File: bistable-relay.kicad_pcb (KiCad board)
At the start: 2 copper layers, 28.8 x 12.9 mm, 11 parts, among them J1 edge_connector, K1 Fujitsu_FTR-F1A, U1 MIC4427

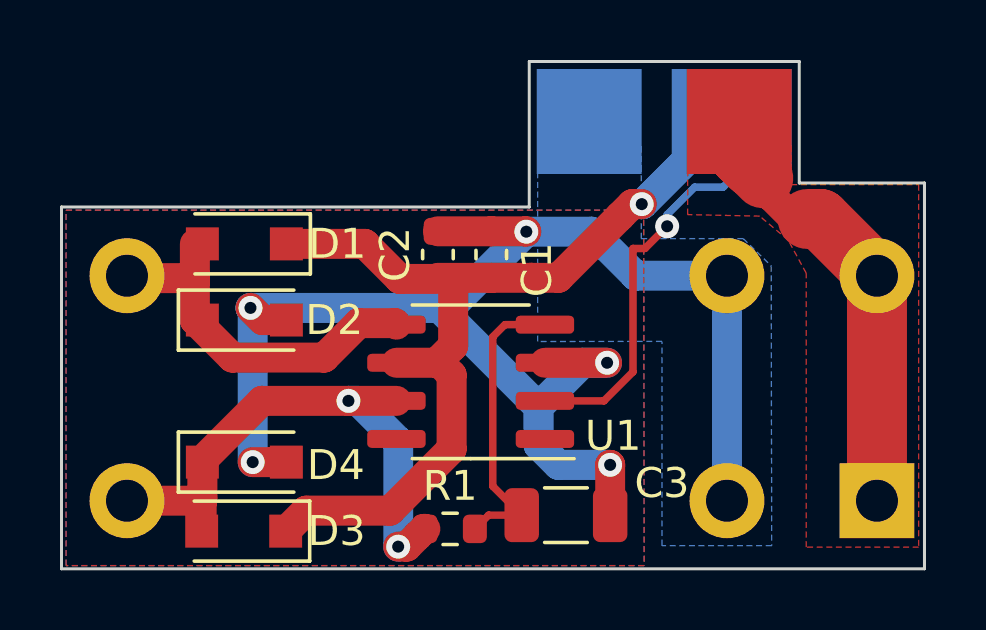
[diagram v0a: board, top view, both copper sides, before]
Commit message: use FH44L relay
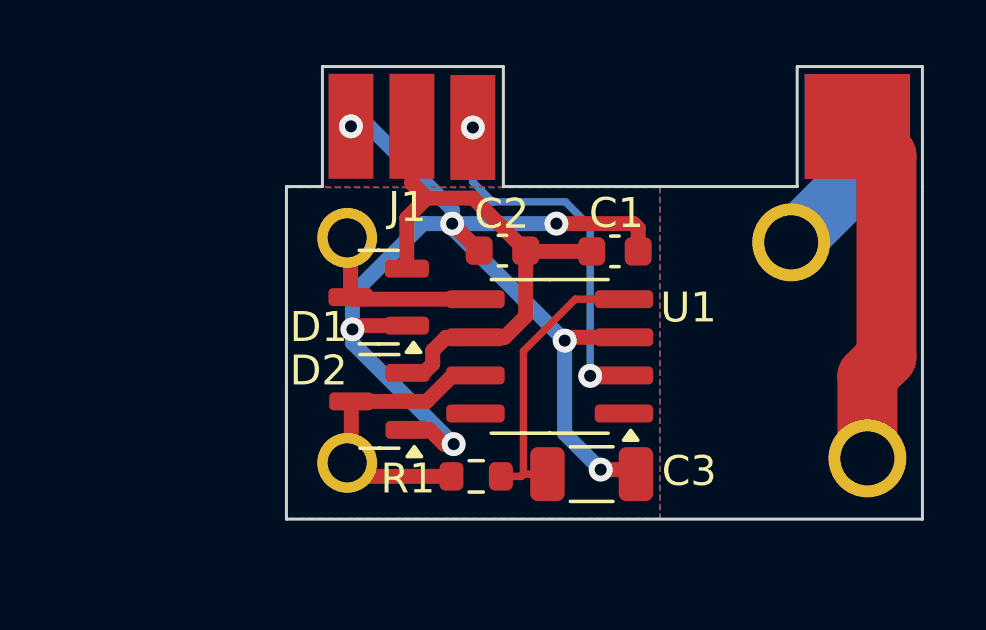
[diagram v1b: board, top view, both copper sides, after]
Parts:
- removed D3, D4: SD103AW, Diode_SMD:D_SOD-123F
- D1, D2: value SD103AW -> BAT54S; footprint Diode_SMD:D_SOD-123F -> Package_TO_SOT_SMD:SOT-23
- J1: moved to F.Cu
- K1: value Fujitsu_FTR-F1A -> FH44L-1AT-L1-DC5V; footprint Relay_THT:Relay_DPST_Fujitsu_FTR-F1A -> Library:RELAY-TH_FH44L-1AT-L1-DC5V
- moved J1 13.1 mm to (151.1, 91.0), turned to 180 degrees
- moved K1 10.3 mm to (140.6, 100.4), turned to 0 degrees
- moved D2 5.25 mm to (133.0, 102.1), turned to 180 degrees
- moved D1 4.82 mm to (132.9, 98.7)
- moved C1 4.12 mm to (140.8, 97.1), turned to 0 degrees
- moved U1 2.77 mm to (138.7, 100.6)
- moved C2 2.15 mm to (137.1, 97.1), turned to 180 degrees
- moved R1 1.95 mm to (136.2, 104.6)
- moved C3 1.61 mm to (140.1, 104.5)
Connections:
- D1 pad 1: VCC -> GND
- D1 pad 2: Net-(D1-Pad2) -> VCC
- D2 pad 1: Net-(D1-Pad2) -> GND
- D2 pad 2: GND -> VCC
- J1 pad 1: GND -> /R1
- J1 pad 2: /OUT -> /R2
- R1 pad 1: Net-(D3-Pad2) -> Net-(D2-COM)
- U1 pad 5: Net-(D1-Pad2) -> Net-(D1-COM)
- U1 pad 7: Net-(D3-Pad2) -> Net-(D2-COM)
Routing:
- net Net-(D3-Pad2): track 19.0 -> 0.00 mm, vias 2 -> 0
- net /OUT: track 16.7 -> 0.00 mm
- net Net-(D1-Pad2): track 12.5 -> 0.00 mm
- net VCC: track 30.7 -> 18.6 mm, vias 1 -> 0
- net /R1: track 0.00 -> 11.7 mm
- net Net-(D2-COM): track 0.00 -> 10.3 mm
- net GND: track 50.9 -> 41.1 mm, vias 5 -> 7
- net Net-(D1-COM): track 0.00 -> 6.21 mm
- net /R2: track 0.00 -> 4.80 mm
- net Net-(J1-REL): track 14.4 -> 12.5 mm, vias 1 -> 2
- removed copper zone on F.Cu, net /OUT
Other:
- board size 28.8 x 12.9 mm -> 21.2 x 11.1 mm

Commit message: move signal pads to bottom layer
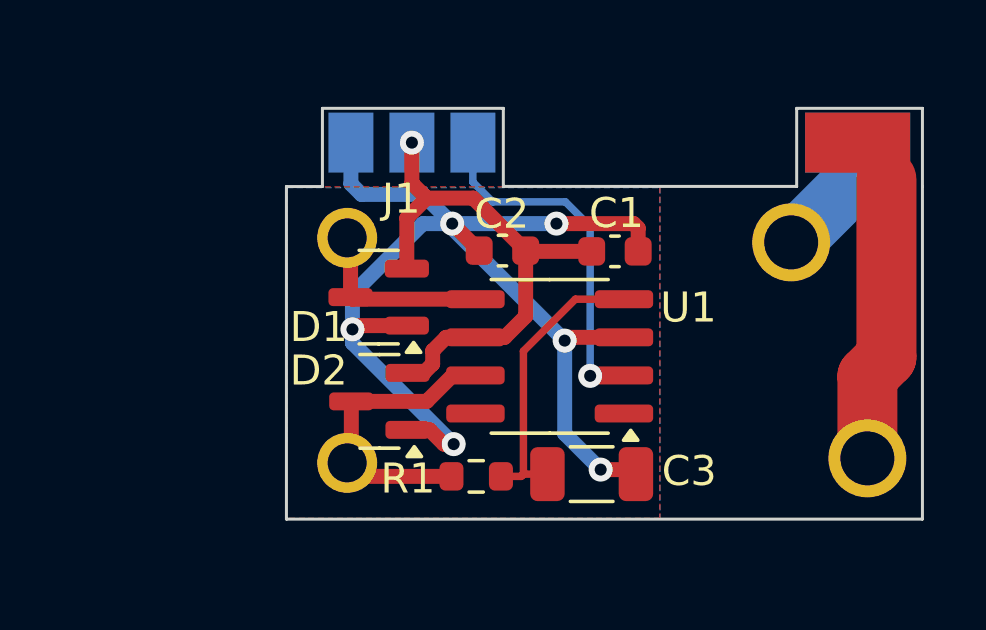
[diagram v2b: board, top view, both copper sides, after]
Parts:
- moved J1 1.29 mm to (151.3, 92.2)
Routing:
- net /R2: track 4.80 -> 3.70 mm
- net /R1: track 11.7 -> 10.9 mm
- net Net-(J1-REL): track 12.5 -> 11.7 mm, vias 2 -> 1
- net VCC: track 18.6 -> 18.1 mm, vias 0 -> 1
- net GND: track 41.1 -> 41.2 mm, vias 7 -> 6
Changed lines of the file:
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@@
 	(footprint "Library:edge_connector"
 		(layer "F.Cu")
-		(at 151.075 90.964 180)
+		(at 151.329 92.23 180)
 		(descr "PCIexpress Bus Edge Connector x1 http://www.ritrontek.com/uploadfile/2016/1026/20161026105231124.pdf#page=70")
 		(tags "PCIe")
 		(property "Reference" "J1"
-			(at 17.175 -4.686 0)
+			(at 17.631 -3.143 0)
 			(layer "F.SilkS")
 			(effects
@@
 		(attr exclude_from_pos_files)
 		(fp_line
-			(start 20 -4)
-			(end 20 0)
+			(start 20.254 -2.73)
+			(end 20.254 -0.127)
 			(stroke
 				(width 0.1)
@@
 		)
 		(fp_line
-			(start 13.97 0)
-			(end 20 0)
+			(start 14.224 -0.127)
+			(end 20.254 -0.127)
 			(stroke
 				(width 0.1)
@@
 		)
 		(fp_line
-			(start 13.97 -4)
-			(end 13.97 0)
+			(start 14.224 -2.73)
+			(end 14.224 -0.127)
 			(stroke
 				(width 0.1)
@@
 		)
 		(fp_line
-			(start 4.174 -4)
-			(end 13.97 -4)
+			(start 4.445 -2.73)
+			(end 14.224 -2.73)
 			(stroke
 				(width 0.1)
@@
 		)
 		(fp_line
-			(start 4.174 -4)
-			(end 4.174 0)
+			(start 4.445 -2.73)
+			(end 4.445 -0.127)
 			(stroke
 				(width 0.1)
@@
 		)
 		(fp_line
-			(start 0 0)
-			(end 4.174 0)
+			(start 0.254 -0.127)
+			(end 4.445 -0.127)
 			(stroke
 				(width 0.1)
@@
 		)
 		(fp_line
-			(start 0 -4)
-			(end 0 0)
+			(start 0.254 -2.73)
+			(end 0.254 -0.127)
 			(stroke
 				(width 0.1)
@@
 		)
 		(fp_line
-			(start 20.2 0.5)
-			(end 20.2 -4)
-			(stroke
-				(width 0.05)
-				(type solid)
-			)
-			(layer "F.CrtYd")
-		)
-		(fp_line
-			(start 20.2 0.5)
-			(end -0.2 0.5)
-			(stroke
-				(width 0.05)
-				(type solid)
-			)
-			(layer "F.CrtYd")
-		)
-		(fp_line
-			(start -0.2 -4)
-			(end 20.2 -4)
-			(stroke
-				(width 0.05)
-				(type solid)
-			)
-			(layer "F.CrtYd")
-		)
-		(fp_line
-			(start -0.2 -4)
-			(end -0.2 0.5)
+			(start 20.454 0)
+			(end 20.454 -2.73)
+			(stroke
+				(width 0.05)
+				(type solid)
+			)
+			(layer "F.CrtYd")
+		)
+		(fp_line
+			(start 20.454 0)
+			(end 0.054 0)
+			(stroke
+				(width 0.05)
+				(type solid)
+			)
+			(layer "F.CrtYd")
+		)
+		(fp_line
+			(start 0.054 -2.73)
+			(end 20.454 -2.73)
+			(stroke
+				(width 0.05)
+				(type solid)
+			)
+			(layer "F.CrtYd")
+		)
+		(fp_line
+			(start 0.054 -2.73)
+			(end 0.054 0)
 			(stroke
 				(width 0.05)
@@
 		)
 		(fp_text user "PCB Thickness 1 mm"
-			(at 0.45 -8.061 90)
+			(at 0.679 -6.87 90)
 			(layer "Cmts.User")
 			(effects
@@
 		)
 		(pad "1" connect rect
-			(at 2.174 -2 180)
-			(size 3.5 3.5)
+			(at 2.413 -1.27 180)
+			(size 3.5 2)
 			(layers "F.Cu" "F.Mask")
 			(net 7 "/R1")
@@
 		)
 		(pad "2" connect rect
-			(at 2.174 -2 180)
-			(size 3.5 3.5)
+			(at 2.413 -1.27 180)
+			(size 3.5 2)
 			(layers "B.Cu" "B.Mask")
 			(net 6 "/R2")
@@
 		)
 		(pad "3" connect rect
-			(at 14.986 -2.032 180)
-			(size 1.5 3.5)
-			(layers "F.Cu" "F.Mask")
+			(at 15.24 -1.27 180)
+			(size 1.5 2)
+			(layers "B.Cu" "B.Mask")
 			(net 8 "Net-(J1-REL)")
 			(pinfunction "REL")
@@
 		)
 		(pad "4" connect rect
-			(at 17.018 -1.993 180)
-			(size 1.5 3.5)
-			(layers "F.Cu" "F.Mask")
+			(at 17.272 -1.27 180)
+			(size 1.5 2)
+			(layers "B.Cu" "B.Mask")
 			(net 1 "VCC")
 			(pinfunction "VCC")
@@
 		)
 		(pad "5" connect rect
-			(at 19.05 -1.993 180)
-			(size 1.5 3.5)
-			(layers "F.Cu" "F.Mask")
+			(at 19.304 -1.27 180)
+			(size 1.5 2)
+			(layers "B.Cu" "B.Mask")
 			(net 2 "GND")
 			(pinfunction "GND")
@@
 		(at 140.57 100.425)
 		(property "Reference" "K1"
-			(at -5.32 -6.15 0)
+			(at 6.03 3.75 0)
 			(layer "B.SilkS")
 			(effects
@@
 		)
 		(model "${KIPRJMOD}/3dshapes/G5Q_14_EU.step"
-			(hide yes)
 			(offset
 				(xyz -9 -3.75 0)
@@
 	(gr_poly
 		(pts
-			(xy 146.625 95.525) (xy 147.45 94.7) (xy 149.9 94.725) (xy 149.875 94.925) (xy 149.675 95.325) (xy 147.95 97.05)
+			(xy 146.625 95.525) (xy 147.65 94.525) (xy 149.9 94.525) (xy 149.875 94.925) (xy 149.675 95.325)
+			(xy 147.95 97.05)
 		)
 		(stroke
@@
 		(pts
 			(xy 148.25 103.225) (xy 148.25 101.25) (xy 148.275 101) (xy 148.375 100.775) (xy 148.525 100.575)
-			(xy 148.875 100.225) (xy 148.875 94.7) (xy 150.65 94.7) (xy 150.65 93.3) (xy 150.725 93.4) (xy 150.8 93.55)
-			(xy 150.85 93.7) (xy 150.875 93.85) (xy 150.875 100.7) (xy 150.85 100.875) (xy 150.775 101.1) (xy 150.675 101.25)
+			(xy 148.875 100.225) (xy 148.875 94.5) (xy 150.65 94.5) (xy 150.65 94.1) (xy 150.725 94.2) (xy 150.8 94.35)
+			(xy 150.85 94.5) (xy 150.875 94.625) (xy 150.875 100.7) (xy 150.85 100.875) (xy 150.775 101.1) (xy 150.675 101.25)
 			(xy 150.25 101.7) (xy 150.25 103.225)
 		)
@@
 	)
 	(segment
+		(start 134.057 94.857)
+		(end 134.057 93.5)
+		(width 0.5)
+		(layer "F.Cu")
+		(net 1)
+	)
+	(segment
 		(start 136.175 99.99)
 		(end 137.149999 99.99)
@@
 	)
 	(segment
-		(start 134.057 92.957)
-		(end 134.057 94.857)
-		(width 0.5)
-		(layer "F.Cu")
-		(net 1)
-	)
-	(segment
 		(start 135.200001 99.99)
 		(end 136.175 99.99)
@@
 	)
 	(segment
-		(start 134.057 94.857)
-		(end 134.55 95.35)
+		(start 134.55 95.35)
+		(end 134.057 94.857)
 		(width 0.5)
 		(layer "F.Cu")
@@
 		(width 0.5)
 		(layer "F.Cu")
+		(net 1)
+	)
+	(via
+		(at 134.057 93.5)
+		(size 0.8)
+		(drill 0.4)
+		(layers "F.Cu" "B.Cu")
 		(net 1)
 	)
@@
 		(net 2)
 	)
-	(via
-		(at 132.025 92.957)
-		(size 0.8)
-		(drill 0.4)
-		(layers "F.Cu" "B.Cu")
-		(net 2)
-	)
 	(segment
 		(start 135.4 96.2)
@@
 	)
 	(segment
-		(start 135.4 95.725)
-		(end 135.4 96.2)
-		(width 0.5)
-		(layer "B.Cu")
-		(net 2)
-	)
-	(segment
 		(start 132.075 98.55061)
 		(end 132.075 99.725)
@@
 	)
 	(segment
+		(start 134.425 95.225)
+		(end 135.4 96.2)
+		(width 0.5)
+		(layer "B.Cu")
+		(net 2)
+	)
+	(segment
 		(start 139.15 103.2)
 		(end 140.35 104.4)
@@
 	)
 	(segment
+		(start 132.375 95.225)
+		(end 134.425 95.225)
+		(width 0.5)
+		(layer "B.Cu")
+		(net 2)
+	)
+	(segment
 		(start 135.375 103.475)
 		(end 135.45 103.55)
@@
 	)
 	(segment
-		(start 132.025 92.957)
-		(end 132.632 92.957)
-		(width 0.5)
-		(layer "B.Cu")
-		(net 2)
-	)
-	(segment
 		(start 139.15 100.1)
 		(end 139.15 103.2)
@@
 	)
 	(segment
-		(start 132.632 92.957)
-		(end 135.4 95.725)
+		(start 132.025 93.75)
+		(end 132.025 94.875)
+		(width 0.5)
+		(layer "B.Cu")
+		(net 2)
+	)
+	(segment
+		(start 132.025 94.875)
+		(end 132.375 95.225)
 		(width 0.5)
 		(layer "B.Cu")
@@
 		(layer "F.Cu")
 		(net 5)
+	)
+	(segment
+		(start 146.7 96.825)
+		(end 146.75 96.825)
+		(width 2)
+		(layer "B.Cu")
+		(net 6)
 	)
 	(segment
@@
 	(segment
 		(start 148.901 94.674)
-		(end 148.901 92.964)
+		(end 148.901 94.061)
 		(width 2)
 		(layer "B.Cu")
@@
 	)
 	(segment
-		(start 146.7 96.825)
-		(end 146.75 96.825)
-		(width 2)
-		(layer "B.Cu")
-		(net 6)
-	)
-	(segment
-		(start 149.875 93.938)
-		(end 148.901 92.964)
+		(start 148.901 93.75)
+		(end 149.875 94.724)
+		(width 0.2)
+		(layer "F.Cu")
+		(net 7)
+	)
+	(segment
+		(start 149.875 100.65)
+		(end 149.875 94.724)
 		(width 2)
 		(layer "F.Cu")
@@
 		(start 149.24 104.025)
 		(end 149.24 101.285)
-		(width 2)
-		(layer "F.Cu")
-		(net 7)
-	)
-	(segment
-		(start 149.875 100.65)
-		(end 149.875 93.938)
 		(width 2)
 		(layer "F.Cu")
@@
 		(net 8)
 	)
-	(via
-		(at 136.089 92.996)
-		(size 0.8)
-		(drill 0.4)
-		(layers "F.Cu" "B.Cu")
+	(segment
+		(start 136.75 95.475)
+		(end 139.175305 95.475)
+		(width 0.25)
+		(layer "B.Cu")
 		(net 8)
 	)
@@
 	)
 	(segment
-		(start 136.75 95.475)
-		(end 139.175305 95.475)
+		(start 136.089 94.814)
+		(end 136.75 95.475)
 		(width 0.25)
 		(layer "B.Cu")
@@
 	)
 	(segment
-		(start 136.089 92.996)
+		(start 136.089 93.75)
 		(end 136.089 94.814)
 		(width 0.25)
 		(layer "B.Cu")
-		(net 8)
-	)
-	(segment
-		(start 136.089 94.814)
-		(end 136.75 95.475)
-		(width 0.25)
-		(layer "B.Cu")
